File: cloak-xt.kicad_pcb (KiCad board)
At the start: 2 copper layers, 21 parts, among them J1 USB_C_Receptacle_USB2.0, U1 STM32F072CBT6, U2 PRTR5V0U2X, U3 XC6206PxxxMR-Regulator_Linear

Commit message: Init matrix
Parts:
- added D1: D_Small, Diode_SMD:D_SOD-123, F.Cu at (-51.8, 37.1)
- added D10: D_Small, Diode_SMD:D_SOD-123, F.Cu at (-51.8, 67.2)
- added D11: D_Small, Diode_SMD:D_SOD-123, F.Cu at (-51.8, 70.6)
- added D12: D_Small, Diode_SMD:D_SOD-123, F.Cu at (-46.0, 37.1)
- added D13: D_Small, Diode_SMD:D_SOD-123, F.Cu at (-46.0, 40.4)
- added D14: D_Small, Diode_SMD:D_SOD-123, F.Cu at (-46.0, 43.8)
- added D15: D_Small, Diode_SMD:D_SOD-123, F.Cu at (-46.0, 47.1)
- added D16: D_Small, Diode_SMD:D_SOD-123, F.Cu at (-46.0, 50.5)
- added D17: D_Small, Diode_SMD:D_SOD-123, F.Cu at (-46.0, 53.8)
- added D18: D_Small, Diode_SMD:D_SOD-123, F.Cu at (-46.0, 57.2)
- added D19: D_Small, Diode_SMD:D_SOD-123, F.Cu at (-46.0, 60.5)
- added D2: D_Small, Diode_SMD:D_SOD-123, F.Cu at (-51.8, 40.4)
- added D20: D_Small, Diode_SMD:D_SOD-123, F.Cu at (-46.0, 63.9)
- added D21: D_Small, Diode_SMD:D_SOD-123, F.Cu at (-46.0, 67.2)
- added D22: D_Small, Diode_SMD:D_SOD-123, F.Cu at (-46.0, 70.6)
- added D23: D_Small, Diode_SMD:D_SOD-123, F.Cu at (-40.3, 37.1)
- added D24: D_Small, Diode_SMD:D_SOD-123, F.Cu at (-40.3, 40.4)
- added D25: D_Small, Diode_SMD:D_SOD-123, F.Cu at (-40.3, 43.8)
- added D26: D_Small, Diode_SMD:D_SOD-123, F.Cu at (-40.3, 47.1)
- added D27: D_Small, Diode_SMD:D_SOD-123, F.Cu at (-40.3, 50.5)
- added D28: D_Small, Diode_SMD:D_SOD-123, F.Cu at (-40.3, 53.8)
- added D29: D_Small, Diode_SMD:D_SOD-123, F.Cu at (-40.3, 57.2)
- added D3: D_Small, Diode_SMD:D_SOD-123, F.Cu at (-51.8, 43.8)
- added D30: D_Small, Diode_SMD:D_SOD-123, F.Cu at (-40.3, 60.5)
- added D31: D_Small, Diode_SMD:D_SOD-123, F.Cu at (-40.3, 63.9)
- added D32: D_Small, Diode_SMD:D_SOD-123, F.Cu at (-40.3, 67.2)
- added D33: D_Small, Diode_SMD:D_SOD-123, F.Cu at (-40.3, 70.6)
- added D34: D_Small, Diode_SMD:D_SOD-123, F.Cu at (-34.5, 37.1)
- added D35: D_Small, Diode_SMD:D_SOD-123, F.Cu at (-34.5, 40.4)
- added D36: D_Small, Diode_SMD:D_SOD-123, F.Cu at (-34.5, 43.8)
- added D37: D_Small, Diode_SMD:D_SOD-123, F.Cu at (-34.5, 47.1)
- added D38: D_Small, Diode_SMD:D_SOD-123, F.Cu at (-34.5, 50.5)
- added D39: D_Small, Diode_SMD:D_SOD-123, F.Cu at (-34.5, 53.8)
- added D4: D_Small, Diode_SMD:D_SOD-123, F.Cu at (-51.8, 47.1)
- added D40: D_Small, Diode_SMD:D_SOD-123, F.Cu at (-34.5, 57.2)
- added D41: D_Small, Diode_SMD:D_SOD-123, F.Cu at (-34.5, 60.5)
- added D42: D_Small, Diode_SMD:D_SOD-123, F.Cu at (-34.5, 63.9)
- added D43: D_Small, Diode_SMD:D_SOD-123, F.Cu at (-34.5, 67.2)
- added D44: D_Small, Diode_SMD:D_SOD-123, F.Cu at (-34.5, 70.6)
- added D45: D_Small, Diode_SMD:D_SOD-123, F.Cu at (-28.7, 37.1)
- added D46: D_Small, Diode_SMD:D_SOD-123, F.Cu at (-28.7, 40.4)
- added D47: D_Small, Diode_SMD:D_SOD-123, F.Cu at (-28.7, 43.8)
- added D48: D_Small, Diode_SMD:D_SOD-123, F.Cu at (-28.7, 47.1)
- added D49: D_Small, Diode_SMD:D_SOD-123, F.Cu at (-28.7, 50.5)
- added D5: D_Small, Diode_SMD:D_SOD-123, F.Cu at (-51.8, 50.5)
- added D50: D_Small, Diode_SMD:D_SOD-123, F.Cu at (-28.7, 53.8)
- added D51: D_Small, Diode_SMD:D_SOD-123, F.Cu at (-28.7, 57.2)
- added D52: D_Small, Diode_SMD:D_SOD-123, F.Cu at (-28.7, 60.5)
- added D53: D_Small, Diode_SMD:D_SOD-123, F.Cu at (-28.7, 63.9)
- added D54: D_Small, Diode_SMD:D_SOD-123, F.Cu at (-28.7, 67.2)
- added D55: D_Small, Diode_SMD:D_SOD-123, F.Cu at (-28.7, 70.6)
- added D56: D_Small, Diode_SMD:D_SOD-123, F.Cu at (-22.9, 37.1)
- added D57: D_Small, Diode_SMD:D_SOD-123, F.Cu at (-22.9, 40.4)
- added D58: D_Small, Diode_SMD:D_SOD-123, F.Cu at (-22.9, 43.8)
- added D59: D_Small, Diode_SMD:D_SOD-123, F.Cu at (-22.9, 47.1)
- added D6: D_Small, Diode_SMD:D_SOD-123, F.Cu at (-51.8, 53.8)
- added D60: D_Small, Diode_SMD:D_SOD-123, F.Cu at (-22.9, 50.5)
- added D61: D_Small, Diode_SMD:D_SOD-123, F.Cu at (-22.9, 53.8)
- added D62: D_Small, Diode_SMD:D_SOD-123, F.Cu at (-22.9, 57.2)
- added D63: D_Small, Diode_SMD:D_SOD-123, F.Cu at (-22.9, 60.5)
- added D64: D_Small, Diode_SMD:D_SOD-123, F.Cu at (-22.9, 63.9)
- added D65: D_Small, Diode_SMD:D_SOD-123, F.Cu at (-22.9, 67.2)
- added D7: D_Small, Diode_SMD:D_SOD-123, F.Cu at (-51.8, 57.2)
- added D8: D_Small, Diode_SMD:D_SOD-123, F.Cu at (-51.8, 60.5)
- added D9: D_Small, Diode_SMD:D_SOD-123, F.Cu at (-51.8, 63.9)
- added MX1: MX_SW_HS, PCM_marbastlib-mx:SW_MX_HS_CPG151101S11_1u, F.Cu at (30.0, 26.8)
- added MX10: MX_SW_HS, PCM_marbastlib-mx:SW_MX_HS_CPG151101S11_1u, F.Cu at (220.5, 26.8)
- added MX11: MX_SW_HS, PCM_marbastlib-mx:SW_MX_HS_CPG151101S11_1u, F.Cu at (239.6, 26.8)
- added MX12: MX_SW_HS, PCM_marbastlib-mx:SW_MX_HS_CPG151101S11_1u, F.Cu at (258.6, 26.8)
- added MX13: MX_SW_HS, PCM_marbastlib-mx:SW_MX_HS_CPG151101S11_1u, F.Cu at (277.7, 26.8)
- added MX14: MX_SW_HS, PCM_marbastlib-mx:SW_MX_HS_CPG151101S11_1u, F.Cu at (301.5, 26.8)
- added MX15: MX_SW_HS, PCM_marbastlib-mx:SW_MX_HS_CPG151101S11_1u, F.Cu at (34.8, 50.6)
- added MX16: MX_SW_HS, PCM_marbastlib-mx:SW_MX_HS_CPG151101S11_1u, F.Cu at (58.6, 50.6)
- added MX17: MX_SW_HS, PCM_marbastlib-mx:SW_MX_HS_CPG151101S11_1u, F.Cu at (77.6, 50.6)
- added MX18: MX_SW_HS, PCM_marbastlib-mx:SW_MX_HS_CPG151101S11_1u, F.Cu at (96.7, 50.6)
- added MX19: MX_SW_HS, PCM_marbastlib-mx:SW_MX_HS_CPG151101S11_1u, F.Cu at (115.7, 50.6)
- added MX2: MX_SW_HS, PCM_marbastlib-mx:SW_MX_HS_CPG151101S11_1u, F.Cu at (53.8, 26.8)
- added MX20: MX_SW_HS, PCM_marbastlib-mx:SW_MX_HS_CPG151101S11_1u, F.Cu at (134.8, 50.6)
- added MX21: MX_SW_HS, PCM_marbastlib-mx:SW_MX_HS_CPG151101S11_1u, F.Cu at (153.8, 50.6)
- added MX22: MX_SW_HS, PCM_marbastlib-mx:SW_MX_HS_CPG151101S11_1u, F.Cu at (172.9, 50.6)
- added MX23: MX_SW_HS, PCM_marbastlib-mx:SW_MX_HS_CPG151101S11_1u, F.Cu at (191.9, 50.6)
- added MX24: MX_SW_HS, PCM_marbastlib-mx:SW_MX_HS_CPG151101S11_1u, F.Cu at (211.0, 50.6)
- added MX25: MX_SW_HS, PCM_marbastlib-mx:SW_MX_HS_CPG151101S11_1u, F.Cu at (230.0, 50.6)
- added MX26: MX_SW_HS, PCM_marbastlib-mx:SW_MX_HS_CPG151101S11_1u, F.Cu at (253.8, 50.6)
- added MX27: MX_SW_HS, PCM_marbastlib-mx:SW_MX_HS_CPG151101S11_1u, F.Cu at (277.7, 50.6)
- added MX28: MX_SW_HS, PCM_marbastlib-mx:SW_MX_HS_CPG151101S11_1u, F.Cu at (301.5, 50.6)
- added MX29: MX_SW_HS, PCM_marbastlib-mx:SW_MX_HS_CPG151101S11_1.75u, F.Cu at (32.4, 69.7)
- added MX3: MX_SW_HS, PCM_marbastlib-mx:SW_MX_HS_CPG151101S11_1u, F.Cu at (72.9, 26.8)
- added MX30: MX_SW_HS, PCM_marbastlib-mx:SW_MX_HS_CPG151101S11_1.75u_STP_1.5, F.Cu at (37.1, 69.7)
- added MX31: MX_SW_HS, PCM_marbastlib-mx:SW_MX_HS_CPG151101S11_1u, F.Cu at (63.3, 69.7)
- added MX32: MX_SW_HS, PCM_marbastlib-mx:SW_MX_HS_CPG151101S11_1u, F.Cu at (82.4, 69.7)
- added MX33: MX_SW_HS, PCM_marbastlib-mx:SW_MX_HS_CPG151101S11_1u, F.Cu at (101.4, 69.7)
- added MX34: MX_SW_HS, PCM_marbastlib-mx:SW_MX_HS_CPG151101S11_1u, F.Cu at (120.5, 69.7)
- added MX35: MX_SW_HS, PCM_marbastlib-mx:SW_MX_HS_CPG151101S11_1u, F.Cu at (139.5, 69.7)
- added MX36: MX_SW_HS, PCM_marbastlib-mx:SW_MX_HS_CPG151101S11_1u, F.Cu at (158.6, 69.7)
- added MX37: MX_SW_HS, PCM_marbastlib-mx:SW_MX_HS_CPG151101S11_1u, F.Cu at (177.6, 69.7)
- added MX38: MX_SW_HS, PCM_marbastlib-mx:SW_MX_HS_CPG151101S11_1u, F.Cu at (196.7, 69.7)
- added MX39: MX_SW_HS, PCM_marbastlib-mx:SW_MX_HS_CPG151101S11_1u, F.Cu at (215.7, 69.7)
- added MX4: MX_SW_HS, PCM_marbastlib-mx:SW_MX_HS_CPG151101S11_1u, F.Cu at (91.9, 26.8)
- added MX40: MX_SW_HS, PCM_marbastlib-mx:SW_MX_HS_CPG151101S11_1u, F.Cu at (234.8, 69.7)
- added MX41: MX_SW_HS, PCM_marbastlib-mx:SW_MX_HS_CPG151101S11_1u, F.Cu at (265.8, 69.7)
- added MX42: MX_SW_HS, PCM_marbastlib-mx:SW_MX_HS_CPG151101S11_1u, F.Cu at (301.5, 69.7)
- added MX43: MX_SW_HS, PCM_marbastlib-mx:SW_MX_HS_CPG151101S11_1u, F.Cu at (32.4, 88.7)
- added MX44: MX_SW_HS, PCM_marbastlib-mx:SW_MX_HS_CPG151101S11_1.25u, F.Cu at (41.9, 88.7)
- added MX45: MX_SW_HS, PCM_marbastlib-mx:SW_MX_HS_CPG151101S11_1u, F.Cu at (53.8, 88.7)
- added MX46: MX_SW_HS, PCM_marbastlib-mx:SW_MX_HS_CPG151101S11_1u, F.Cu at (72.9, 88.7)
- added MX47: MX_SW_HS, PCM_marbastlib-mx:SW_MX_HS_CPG151101S11_1u, F.Cu at (91.9, 88.7)
- added MX48: MX_SW_HS, PCM_marbastlib-mx:SW_MX_HS_CPG151101S11_1u, F.Cu at (111.0, 88.7)
- added MX49: MX_SW_HS, PCM_marbastlib-mx:SW_MX_HS_CPG151101S11_1u, F.Cu at (130.0, 88.7)
- added MX5: MX_SW_HS, PCM_marbastlib-mx:SW_MX_HS_CPG151101S11_1u, F.Cu at (111.0, 26.8)
- added MX50: MX_SW_HS, PCM_marbastlib-mx:SW_MX_HS_CPG151101S11_1u, F.Cu at (149.1, 88.7)
- added MX51: MX_SW_HS, PCM_marbastlib-mx:SW_MX_HS_CPG151101S11_1u, F.Cu at (168.1, 88.7)
- added MX52: MX_SW_HS, PCM_marbastlib-mx:SW_MX_HS_CPG151101S11_1u, F.Cu at (187.2, 88.7)
- added MX53: MX_SW_HS, PCM_marbastlib-mx:SW_MX_HS_CPG151101S11_1u, F.Cu at (206.2, 88.7)
- added MX54: MX_SW_HS, PCM_marbastlib-mx:SW_MX_HS_CPG151101S11_1u, F.Cu at (225.3, 88.7)
- added MX55: MX_SW_HS, PCM_marbastlib-mx:SW_MX_HS_CPG151101S11_1u, F.Cu at (244.3, 88.7)
- added MX56: MX_SW_HS, PCM_marbastlib-mx:SW_MX_HS_CPG151101S11_1u, F.Cu at (270.5, 88.7)
- added MX57: MX_SW_HS, PCM_marbastlib-mx:SW_MX_HS_CPG151101S11_1u, F.Cu at (301.5, 88.7)
- added MX58: MX_SW_HS, PCM_marbastlib-mx:SW_MX_HS_CPG151101S11_1u, F.Cu at (34.8, 107.8)
- added MX59: MX_SW_HS, PCM_marbastlib-mx:SW_MX_HS_CPG151101S11_1u, F.Cu at (58.6, 107.8)
- added MX6: MX_SW_HS, PCM_marbastlib-mx:SW_MX_HS_CPG151101S11_1u, F.Cu at (137.3, 26.8)
- added MX60: MX_SW_HS, PCM_marbastlib-mx:SW_MX_HS_CPG151101S11_1u, F.Cu at (77.6, 107.8)
- added MX61: MX_SW_HS, PCM_marbastlib-mx:SW_MX_HS_CPG151101S11_1u, F.Cu at (82.4, 107.8)
- added MX62: MX_SW_HS, PCM_marbastlib-mx:SW_MX_HS_CPG151101S11_1u, F.Cu at (125.3, 107.8)
- added MX63: MX_SW_HS, PCM_marbastlib-mx:SW_MX_HS_CPG151101S11_1u, F.Cu at (153.8, 107.8)
- added MX64: MX_SW_HS, PCM_marbastlib-mx:SW_MX_HS_CPG151101S11_1u, F.Cu at (182.4, 107.8)
- added MX65: MX_SW_HS, PCM_marbastlib-mx:SW_MX_HS_CPG151101S11_1u, F.Cu at (225.3, 107.8)
- added MX66: MX_SW_HS, PCM_marbastlib-mx:SW_MX_HS_CPG151101S11_1u, F.Cu at (230.0, 107.8)
- added MX67: MX_SW_HS, PCM_marbastlib-mx:SW_MX_HS_CPG151101S11_1u, F.Cu at (249.1, 107.8)
- added MX68: MX_SW_HS, PCM_marbastlib-mx:SW_MX_HS_CPG151101S11_1u, F.Cu at (272.9, 107.8)
- added MX69: MX_SW_HS, PCM_marbastlib-mx:SW_MX_HS_CPG151101S11_1u, F.Cu at (301.5, 107.8)
- added MX7: MX_SW_HS, PCM_marbastlib-mx:SW_MX_HS_CPG151101S11_1u, F.Cu at (156.3, 26.8)
- added MX8: MX_SW_HS, PCM_marbastlib-mx:SW_MX_HS_CPG151101S11_1u, F.Cu at (175.4, 26.8)
- added MX9: MX_SW_HS, PCM_marbastlib-mx:SW_MX_HS_CPG151101S11_1u, F.Cu at (194.4, 26.8)
- moved BOOT1 218.2 mm to (351.0, 103.7)
- moved C1 218.2 mm to (355.5, 94.4)
- moved C10 218.2 mm to (351.3, 78.9)
- moved C2 218.2 mm to (348.5, 79.2)
- moved C3 218.2 mm to (349.8, 82.2)
- moved C4 218.2 mm to (358.5, 82.4)
- moved C5 218.2 mm to (349.5, 90.9)
- moved C6 218.2 mm to (350.0, 92.4)
- moved C7 218.2 mm to (355.5, 93.1)
- moved C8 218.2 mm to (351.0, 72.2)
- moved C9 218.2 mm to (352.5, 75.4)
- moved F1 218.2 mm to (354.0, 73.2)
- moved J1 218.2 mm to (354.0, 60.9)
- moved R1 218.2 mm to (351.0, 70.2)
- moved R2 218.2 mm to (351.0, 67.7)
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
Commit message: Update PCB from schematics
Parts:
- added S1: 6u, PCM_marbastlib-mx:STAB_MX_P_6u, F.Cu at (229.5, 165.1)
- added S41: 2.25u, PCM_marbastlib-mx:STAB_MX_P_2.25u, F.Cu at (341.4, 127.0)
- added S44: 2.25u, PCM_marbastlib-mx:STAB_MX_P_2.25u, F.Cu at (117.5, 146.0)
- added S63: 3u, PCM_marbastlib-mx:STAB_MX_P_3u, F.Cu at (258.0, 165.1)
- added S64: 7u, PCM_marbastlib-mx:STAB_MX_P_7u, F.Cu at (229.5, 165.1)
- added S65: 3u, PCM_marbastlib-mx:STAB_MX_P_3u, F.Cu at (200.9, 165.1)
- MX1, MX10, MX11, MX12, MX13, MX14, MX16, MX17, MX18, MX19, MX2, MX20, MX21, MX22, MX23, MX24, MX25, MX27, MX28, MX3, MX31, MX32, MX33, MX34, MX35, MX36, MX37, MX38, MX39, MX4, MX40, MX41, MX42, MX45, MX46, MX47, MX48, MX49, MX5, MX50, MX51, MX52, MX53, MX54, MX55, MX57, MX6, MX61, MX62, MX63, MX64, MX65, MX66, MX67, MX69, MX7, MX8, MX9: moved to B.Cu
- MX15, MX26, MX58, MX59, MX60, MX68: footprint PCM_marbastlib-mx:SW_MX_HS_CPG151101S11_1u -> PCM_marbastlib-mx:SW_MX_HS_CPG151101S11_1.5u; moved to B.Cu
- MX29: footprint PCM_marbastlib-mx:SW_MX_HS_CPG151101S11_1.75u -> PCM_marbastlib-mx:SW_MX_HS_CPG151101S11_1.75u_STP_1.25; moved to B.Cu
- MX30: footprint PCM_marbastlib-mx:SW_MX_HS_CPG151101S11_1.75u_STP_1.5 -> PCM_marbastlib-mx:SW_MX_HS_CPG151101S11_1.75u; moved to B.Cu
- MX43: footprint PCM_marbastlib-mx:SW_MX_HS_CPG151101S11_1u -> PCM_marbastlib-mx:SW_MX_HS_CPG151101S11_1.25u; moved to B.Cu
- MX44: footprint PCM_marbastlib-mx:SW_MX_HS_CPG151101S11_1.25u -> PCM_marbastlib-mx:SW_MX_HS_CPG151101S11_1u; moved to B.Cu
- MX56: footprint PCM_marbastlib-mx:SW_MX_HS_CPG151101S11_1u -> PCM_marbastlib-mx:SW_MX_HS_CPG151101S11_1.75u; moved to B.Cu
- moved BOOT1 473.6 mm to (-107.9, 220.8)
- moved C1 473.6 mm to (-103.3, 211.6)
- moved C10 473.6 mm to (-107.6, 196.1)
- moved C2 473.6 mm to (-110.4, 196.3)
- moved C3 473.6 mm to (-109.1, 199.3)
- moved C4 473.6 mm to (-100.4, 199.6)
- moved C5 473.6 mm to (-109.4, 208.1)
- moved C6 473.6 mm to (-108.9, 209.6)
- moved C7 473.6 mm to (-103.3, 210.3)
- moved C8 473.6 mm to (-107.9, 189.3)
- moved C9 473.6 mm to (-106.4, 192.6)
- moved F1 473.6 mm to (-104.9, 190.3)
- moved J1 473.6 mm to (-104.9, 178.1)
- moved R1 473.6 mm to (-107.9, 187.3)
- moved R2 473.6 mm to (-107.9, 184.8)
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
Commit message: Fixed diodes notation
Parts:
- removed D30, D44, D61: D_Small, Diode_SMD:D_SOD-123
- removed S65: 3u, PCM_marbastlib-mx:STAB_MX_P_3u
- added D67: D_Small, Diode_SMD:D_SOD-123, F.Cu at (327.9, 165.9)
- added D68: D_Small, Diode_SMD:D_SOD-123, F.Cu at (351.7, 165.9)
- added D69: D_Small, Diode_SMD:D_SOD-123, F.Cu at (380.3, 165.9)
- added S62: 3u, PCM_marbastlib-mx:STAB_MX_P_3u, F.Cu at (200.9, 165.1)
- D1, D10, D11, D12, D13, D14, D15, D16, D17, D18, D19, D2, D20, D21, D22, D23, D24, D25, D26, D27, D28, D29, D3, D31, D32, D33, D34, D35, D36, D37, D38, D39, D4, D40, D41, D42, D43, D45, D46, D47, D48, D49, D5, D50, D51, D52, D53, D54, D55, D56, D57, D58, D59, D6, D60, D62, D63, D64, D65, D7, D8, D9: moved to B.Cu
- MX59, MX60: footprint PCM_marbastlib-mx:SW_MX_HS_CPG151101S11_1.5u -> PCM_marbastlib-mx:SW_MX_HS_CPG151101S11_1u
- MX61, MX66: footprint PCM_marbastlib-mx:SW_MX_HS_CPG151101S11_1u -> PCM_marbastlib-mx:SW_MX_HS_CPG151101S11_1.5u
- S63: value 3u -> 7u; footprint PCM_marbastlib-mx:STAB_MX_P_3u -> PCM_marbastlib-mx:STAB_MX_P_7u
- S64: value 7u -> 3u; footprint PCM_marbastlib-mx:STAB_MX_P_7u -> PCM_marbastlib-mx:STAB_MX_P_3u
- moved D58 251.5 mm to (113.6, 165.9), turned to 90 degrees
- moved D59 235.9 mm to (137.4, 165.9), turned to 90 degrees
- moved D57 227.8 mm to (380.3, 146.8), turned to 90 degrees
- moved D45 227.6 mm to (132.6, 146.8), turned to 90 degrees
- moved D60 223.9 mm to (156.4, 165.9), turned to 90 degrees
- moved D56 215.6 mm to (349.3, 146.8), turned to 90 degrees
- moved D46 215.4 mm to (151.7, 146.8), turned to 90 degrees
- moved D43 212.0 mm to (111.2, 146.8), turned to 90 degrees
- moved D47 204.2 mm to (170.7, 146.8), turned to 90 degrees
- moved D29 201.3 mm to (111.2, 127.8), turned to 90 degrees
- moved D42 201.2 mm to (380.3, 127.8), turned to 90 degrees
- moved D62 200.5 mm to (204.1, 165.9), turned to 90 degrees
- moved D28 198.7 mm to (380.3, 108.7), turned to 90 degrees
- moved D48 194.4 mm to (189.8, 146.8), turned to 90 degrees
- moved D14 193.6 mm to (380.3, 84.9), turned to 90 degrees
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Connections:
- MX31 pad 2: Net-(D30-A) -> Net-(D31-A)
- MX32 pad 2: Net-(D31-A) -> Net-(D32-A)
- MX33 pad 2: Net-(D32-A) -> Net-(D33-A)
- MX34 pad 2: Net-(D33-A) -> Net-(D34-A)
- MX35 pad 2: Net-(D34-A) -> Net-(D35-A)
- MX36 pad 2: Net-(D35-A) -> Net-(D36-A)
- MX37 pad 2: Net-(D36-A) -> Net-(D37-A)
- MX38 pad 2: Net-(D37-A) -> Net-(D38-A)
- MX39 pad 2: Net-(D38-A) -> Net-(D39-A)
- MX40 pad 2: Net-(D39-A) -> Net-(D40-A)
- MX41 pad 2: Net-(D40-A) -> Net-(D41-A)
- MX42 pad 2: Net-(D41-A) -> Net-(D42-A)
- MX44 pad 2: Net-(D42-A) -> Net-(D43-A)
- MX45 pad 2: Net-(D43-A) -> Net-(D45-A)
- MX46 pad 2: Net-(D44-A) -> Net-(D46-A)
- MX47 pad 2: Net-(D45-A) -> Net-(D47-A)
- MX48 pad 2: Net-(D46-A) -> Net-(D48-A)
- MX49 pad 2: Net-(D47-A) -> Net-(D49-A)
- MX50 pad 2: Net-(D48-A) -> Net-(D50-A)
- MX51 pad 2: Net-(D49-A) -> Net-(D51-A)
- MX52 pad 2: Net-(D50-A) -> Net-(D52-A)
- MX53 pad 2: Net-(D51-A) -> Net-(D53-A)
- MX54 pad 2: Net-(D52-A) -> Net-(D54-A)
- MX55 pad 2: Net-(D53-A) -> Net-(D55-A)
- MX56 pad 2: Net-(D54-A) -> Net-(D56-A)
- MX57 pad 2: Net-(D55-A) -> Net-(D57-A)
- MX58 pad 2: unconnected-(MX58-Pad2) -> Net-(D58-A)
- MX59 pad 2: unconnected-(MX59-Pad2) -> Net-(D59-A)
- MX60 pad 2: Net-(D56-A) -> Net-(D60-A)
- MX61 pad 2: Net-(D57-A) -> unconnected-(MX61-Pad2)
- MX62 pad 2: Net-(D58-A) -> Net-(D62-A)
- MX63 pad 2: Net-(D59-A) -> Net-(D63-A)
- MX64 pad 2: Net-(D60-A) -> Net-(D64-A)
- MX65 pad 2: Net-(D61-A) -> Net-(D65-A)
- MX66 pad 2: Net-(D62-A) -> unconnected-(MX66-Pad2)
- MX67 pad 2: Net-(D63-A) -> Net-(D67-A)
- MX68 pad 2: Net-(D64-A) -> Net-(D68-A)
- MX69 pad 2: Net-(D65-A) -> Net-(D69-A)

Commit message: Add edge cuts
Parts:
- BOOT1, C1, C10, C2, C3, C4, C5, C6, C7, C8, C9, D67, D68, D69, F1, J1, R1, R2, R3, R4, RST1, U1, U2, U3: moved to B.Cu
- moved C2 191.8 mm to (67.6, 124.9), turned to 0 degrees
- moved C5 189.9 mm to (66.6, 136.6)
- moved C3 189.5 mm to (66.4, 127.9), turned to 0 degrees
- moved U3 189.5 mm to (66.4, 122.1), turned to 180 degrees
- moved C6 189.0 mm to (66.1, 138.1), turned to 0 degrees
- moved BOOT1 187.2 mm to (65.1, 149.4)
- moved C8 187.2 mm to (65.1, 117.9)
- moved R1 187.2 mm to (65.1, 115.9), turned to 180 degrees
- moved R2 187.2 mm to (65.1, 113.4), turned to 0 degrees
- moved C10 186.7 mm to (64.9, 124.6), turned to 180 degrees
- moved C9 184.4 mm to (63.6, 121.1)
- moved R3 183.9 mm to (63.4, 142.4), turned to 180 degrees
- moved F1 181.6 mm to (62.1, 118.9), turned to 0 degrees
- moved J1 181.6 mm to (62.1, 106.6), turned to 0 degrees
- moved U1 181.6 mm to (62.1, 132.4)
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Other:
- board outline added: 289.7 x 98 mm

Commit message: Remove onboard USB/ESD and add JST
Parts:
- moved C1 397.7 mm to (458.4, 138.9)
- moved C7 397.7 mm to (458.4, 137.7)
- moved BOOT1 397.7 mm to (462.9, 148.2)
- moved C10 397.7 mm to (462.6, 123.4)
- moved C2 397.7 mm to (465.4, 123.7)
- moved C3 397.7 mm to (464.1, 126.7)
- moved C4 397.7 mm to (455.4, 126.9)
- moved C5 397.7 mm to (464.4, 135.4)
- moved C6 397.7 mm to (463.9, 136.9)
- moved C8 397.7 mm to (462.9, 116.7)
- moved C9 397.7 mm to (461.4, 119.9)
- moved F1 397.7 mm to (459.9, 117.7)
- moved J1 397.7 mm to (459.9, 105.4)
- moved R1 397.7 mm to (462.9, 114.7)
- moved R2 397.7 mm to (462.9, 112.2)
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
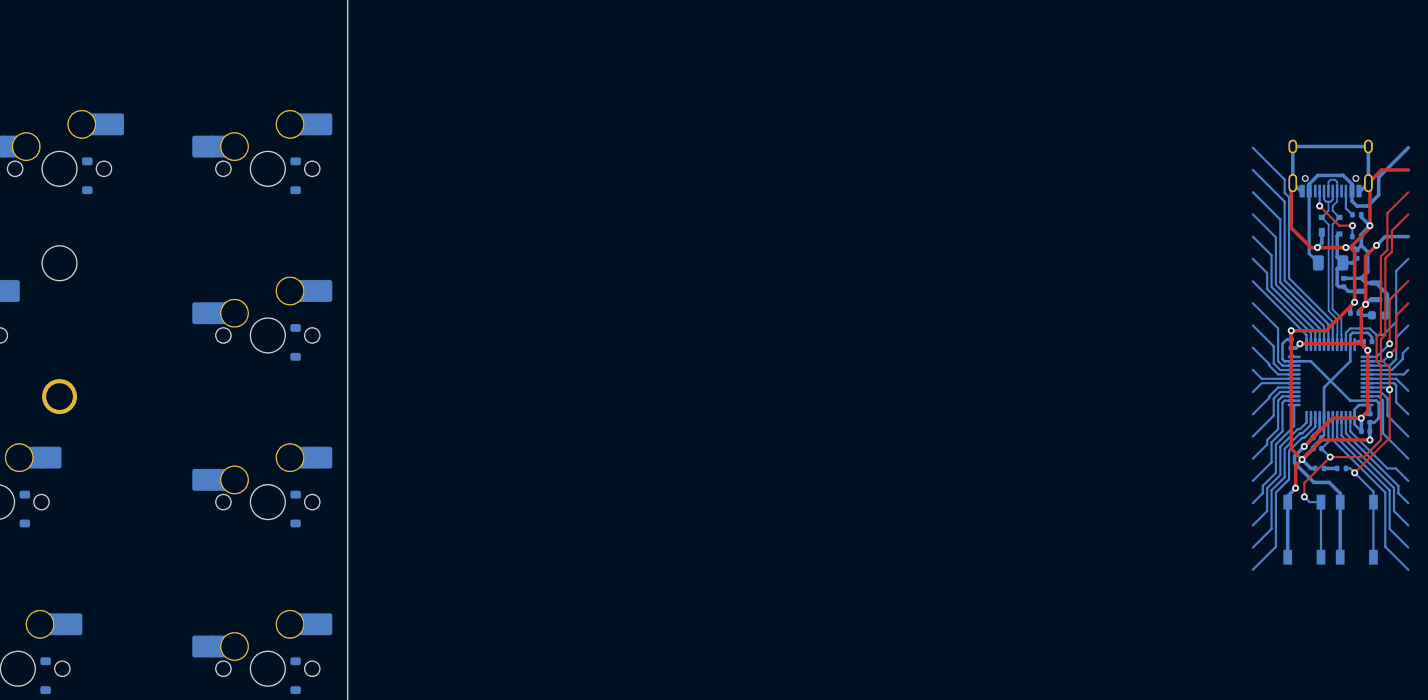
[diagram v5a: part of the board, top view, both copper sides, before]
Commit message: Update JST on PCB
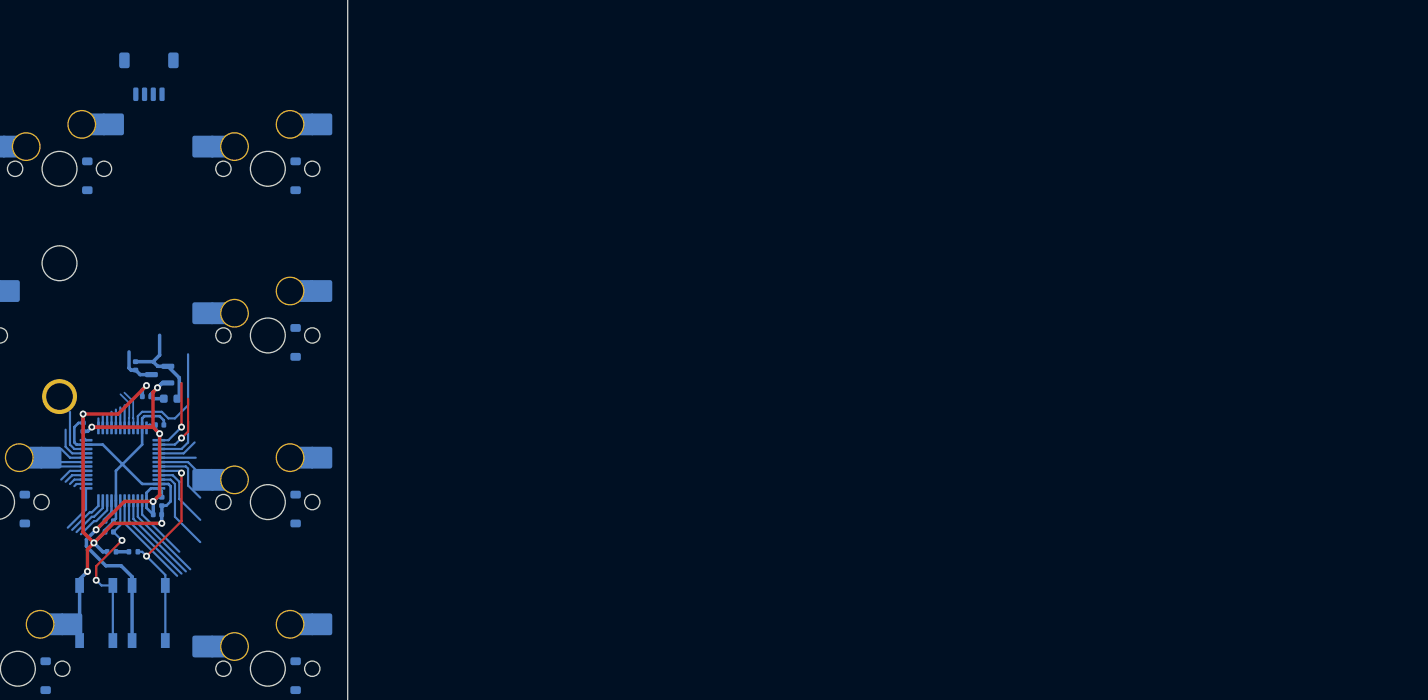
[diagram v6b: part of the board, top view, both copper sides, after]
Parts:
- removed C8: 100nF, Capacitor_SMD:C_0402_1005Metric
- removed F1: 500mA, Fuse:Fuse_1206_3216Metric
- removed R1, R2: 5.1k, Resistor_SMD:R_0402_1005Metric
- removed U2: PRTR5V0U2X, Package_TO_SOT_SMD:SOT-143
- J1: value USB_C_Receptacle_USB2.0 -> JST; footprint Connector_USB:USB_C_Receptacle_HRO_TYPE-C-31-M-12 -> Connector_JST:JST_SH_SM04B-SRSS-TB_1x04-1MP_P1.00mm_Horizontal
- moved C1 138.4 mm to (320.3, 148.4)
- moved C7 138.4 mm to (320.3, 147.2)
- moved BOOT1 138.4 mm to (324.8, 157.7)
- moved C10 138.4 mm to (324.5, 133.0)
- moved C2 138.4 mm to (327.3, 133.2)
- moved C3 138.4 mm to (326.0, 136.2)
- moved C4 138.4 mm to (317.3, 136.5)
- moved C5 138.4 mm to (326.3, 145.0)
- moved C6 138.4 mm to (325.8, 146.5)
- moved C9 138.4 mm to (323.3, 129.5)
- moved R3 138.4 mm to (323.0, 150.7)
- moved R4 138.4 mm to (320.5, 150.7)
- moved RST1 138.4 mm to (318.8, 157.7)
- moved U1 138.4 mm to (321.8, 140.7)
- moved U3 138.4 mm to (326.0, 130.5)
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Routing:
- net GND: track 162.5 -> 100.8 mm, vias 8 -> 5
- net NRST: track 56.2 -> 19.5 mm
- net VBUS: track 27.7 -> 0.00 mm
- net /A10: track 26.3 -> 2.59 mm
- net BOOT0: track 47.3 -> 25.6 mm
- net /A9: track 23.5 -> 2.34 mm
- net /A8: track 20.8 -> 2.09 mm
- net D+: track 22.1 -> 4.45 mm
- net /B15: track 18.0 -> 1.84 mm
- net D-: track 20.5 -> 4.26 mm
- net /A0: track 20.5 -> 5.23 mm
- net /B14: track 15.3 -> 1.59 mm
- net /A1: track 17.8 -> 4.98 mm
- net +3V3: track 78.1 -> 66.8 mm, vias 6 -> 5
- net /B13: track 12.6 -> 1.34 mm
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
